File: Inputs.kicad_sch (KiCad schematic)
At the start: 2 parts, among them J14 Conn_01x30_Socket

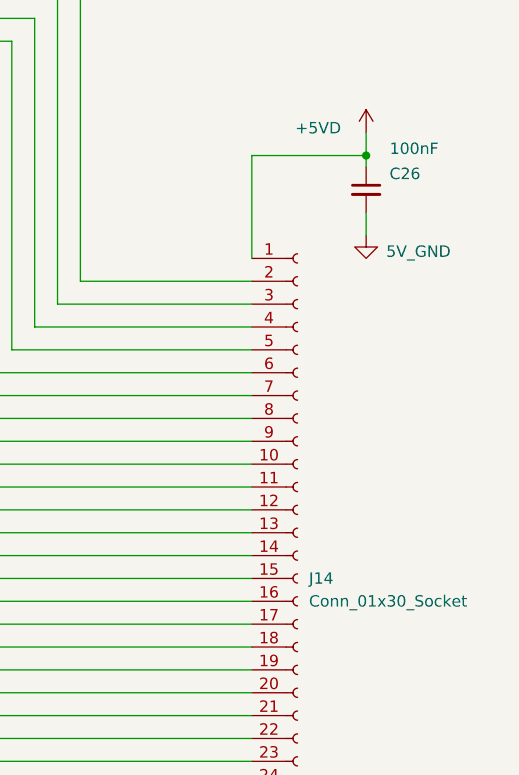
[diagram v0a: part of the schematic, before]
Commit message: Deleted stale test production files. Fixed up a bug with power isolation. Created some footprints for wire to board connectors although ran out of time to fix a bug where they do no lock in. Fixes to readme
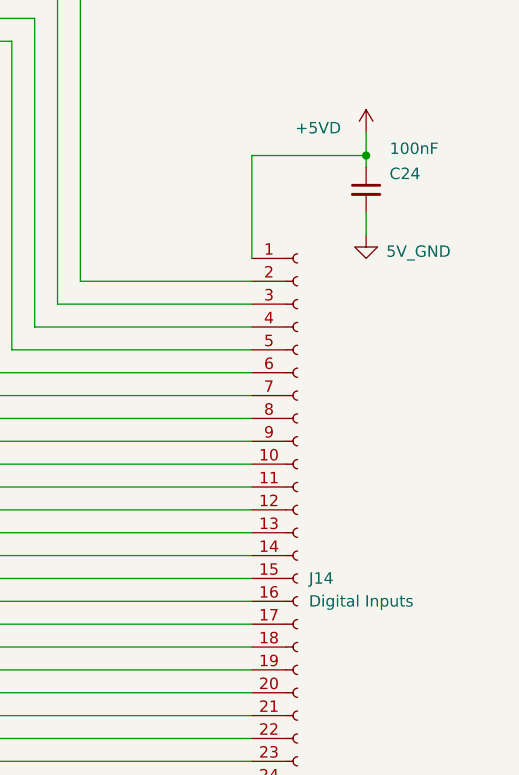
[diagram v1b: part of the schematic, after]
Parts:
- J14: value Conn_01x30_Socket -> Digital Inputs; footprint (none) -> OSTVTerminalBlocks:Conn01x30
- renumbered C26 to C24
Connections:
- net Digital Input ${CH1}&${CH2}/MCU_IP${CH1} is gone; now on net Digital Input ${CH1}&${CH2}/MCU_IP${CH1}: J14.8 (Pin_8)
- net Digital Input ${CH1}&${CH2}/MCU_IP${CH2} is gone; now on net Digital Input ${CH1}&${CH2}/MCU_IP${CH2}: J14.9 (Pin_9)
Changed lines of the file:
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@@
 		(on_board yes)
 		(dnp no)
-		(property "Reference" "#PWR0150"
+		(property "Reference" "#PWR0144"
 			(at 193.04 147.32 0)
 			(effects
@@
 			(project "Remora Nucleo F446ZE Hat"
 				(path "/5473abc6-7b93-43cc-a401-f691c4d7d7cf/181d5939-8311-41b3-8216-f7233e3a75eb"
-					(reference "#PWR0150")
+					(reference "#PWR0144")
 					(unit 1)
 				)
@@
 		(on_board yes)
 		(dnp no)
-		(property "Reference" "#PWR0151"
+		(property "Reference" "#PWR0145"
 			(at 205.74 54.61 0)
 			(effects
@@
 			(project "Remora Nucleo F446ZE Hat"
 				(path "/5473abc6-7b93-43cc-a401-f691c4d7d7cf/181d5939-8311-41b3-8216-f7233e3a75eb"
-					(reference "#PWR0151")
+					(reference "#PWR0145")
 					(unit 1)
 				)
@@
 		(on_board yes)
 		(dnp no)
-		(property "Reference" "C26"
+		(property "Reference" "C24"
 			(at 210.058 55.372 0)
 			(effects
@@
 			(project "Remora Nucleo F446ZE Hat"
 				(path "/5473abc6-7b93-43cc-a401-f691c4d7d7cf/181d5939-8311-41b3-8216-f7233e3a75eb"
-					(reference "C26")
+					(reference "C24")
 					(unit 1)
 				)
@@
 		(on_board yes)
 		(dnp no)
-		(property "Reference" "#PWR0152"
+		(property "Reference" "#PWR0146"
 			(at 205.74 68.58 0)
 			(effects
@@
 			(project "Remora Nucleo F446ZE Hat"
 				(path "/5473abc6-7b93-43cc-a401-f691c4d7d7cf/181d5939-8311-41b3-8216-f7233e3a75eb"
-					(reference "#PWR0152")
+					(reference "#PWR0146")
 					(unit 1)
 				)
@@
 			)
 		)
-		(property "Value" "Conn_01x30_Socket"
+		(property "Value" "Digital Inputs"
 			(at 199.39 102.8699 0)
 			(effects
@@
 			)
 		)
-		(property "Footprint" ""
+		(property "Footprint" "OSTVTerminalBlocks:Conn01x30"
 			(at 198.12 100.33 0)
 			(effects

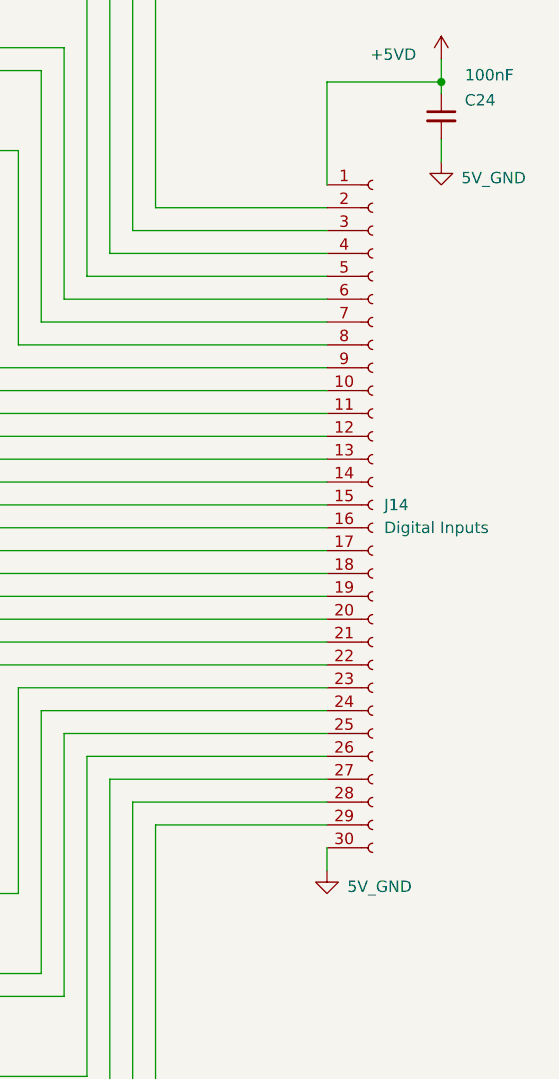
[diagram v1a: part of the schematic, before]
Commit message: restructured power supplies to enable Spindle DAC to be isolated. We now have the option of supplying two 24V inputs, one to power the nucleo and everything logic side and the other to power peripherals. Some testing will be required.
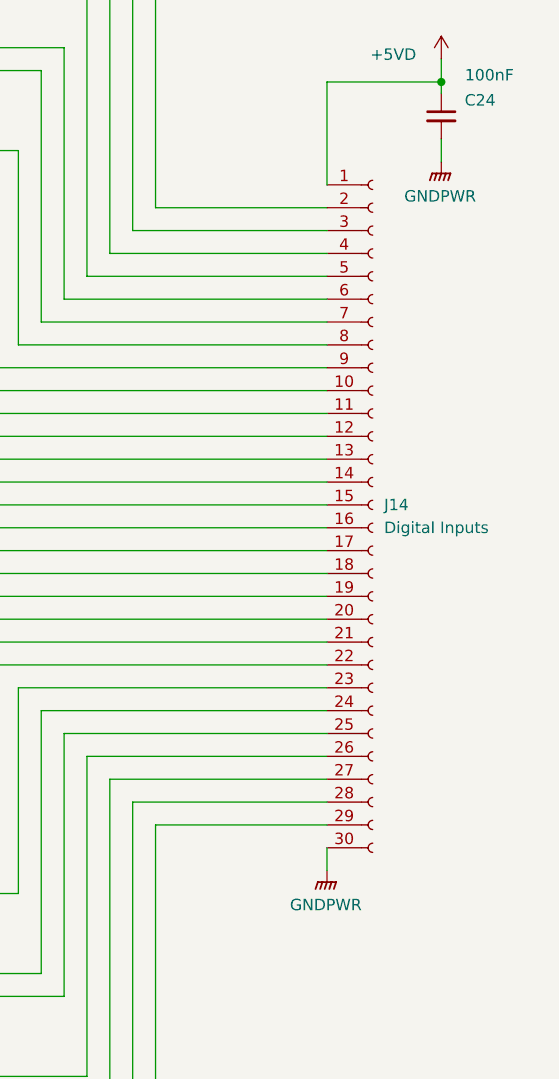
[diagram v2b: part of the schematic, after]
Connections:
- net Digital Input ${CH1}&${CH2}/MCU_IP${CH1} is gone; now on net Digital Input ${CH1}&${CH2}/MCU_IP${CH1}: J14.8 (Pin_8)
- net Digital Input ${CH1}&${CH2}/MCU_IP${CH2} is gone; now on net Digital Input ${CH1}&${CH2}/MCU_IP${CH2}: J14.9 (Pin_9)
- net 5V_GND renamed GNDPWR
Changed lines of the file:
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@@
-	)
-	(symbol
-		(lib_id "power:GND1")
-		(at 193.04 140.97 0)
-		(unit 1)
-		(exclude_from_sim no)
-		(in_bom yes)
-		(on_board yes)
-		(dnp no)
-		(property "Reference" "#PWR0144"
-			(at 193.04 147.32 0)
-			(effects
-				(font
-					(size 1.27 1.27)
-				)
-				(hide yes)
-			)
-		)
-		(property "Value" "5V_GND"
-			(at 198.882 142.748 0)
-			(effects
-				(font
-					(size 1.27 1.27)
-				)
-			)
-		)
-		(property "Footprint" ""
-			(at 193.04 140.97 0)
-			(effects
-				(font
-					(size 1.27 1.27)
-				)
-				(hide yes)
-			)
-		)
-		(property "Datasheet" ""
-			(at 193.04 140.97 0)
-			(effects
-				(font
-					(size 1.27 1.27)
-				)
-				(hide yes)
-			)
-		)
-		(property "Description" "Power symbol creates a global label with name \"GND1\" , ground"
-			(at 193.04 140.97 0)
-			(effects
-				(font
-					(size 1.27 1.27)
-				)
-				(hide yes)
-			)
-		)
-		(pin "1"
-		)
-		(instances
-			(project "Remora Nucleo F446ZE Hat"
-				(path "/5473abc6-7b93-43cc-a401-f691c4d7d7cf/181d5939-8311-41b3-8216-f7233e3a75eb"
-					(reference "#PWR0144")
-					(unit 1)
-				)
-			)
-		)
 	)
 	(symbol
@@
 	)
 	(symbol
+		(lib_id "power:GNDPWR")
+		(at 193.04 140.97 0)
+		(unit 1)
+		(exclude_from_sim no)
+		(in_bom yes)
+		(on_board yes)
+		(dnp no)
+		(fields_autoplaced yes)
+		(property "Reference" "#PWR073"
+			(at 193.04 146.05 0)
+			(effects
+				(font
+					(size 1.27 1.27)
+				)
+				(hide yes)
+			)
+		)
+		(property "Value" "GNDPWR"
+			(at 192.913 144.78 0)
+			(effects
+				(font
+					(size 1.27 1.27)
+				)
+			)
+		)
+		(property "Footprint" ""
+			(at 193.04 142.24 0)
+			(effects
+				(font
+					(size 1.27 1.27)
+				)
+				(hide yes)
+			)
+		)
+		(property "Datasheet" ""
+			(at 193.04 142.24 0)
+			(effects
+				(font
+					(size 1.27 1.27)
+				)
+				(hide yes)
+			)
+		)
+		(property "Description" "Power symbol creates a global label with name \"GNDPWR\" , global ground"
+			(at 193.04 140.97 0)
+			(effects
+				(font
+					(size 1.27 1.27)
+				)
+				(hide yes)
+			)
+		)
+		(pin "1"
+		)
+		(instances
+			(project "Remora Nucleo F446ZE Hat"
+				(path "/5473abc6-7b93-43cc-a401-f691c4d7d7cf/181d5939-8311-41b3-8216-f7233e3a75eb"
+					(reference "#PWR073")
+					(unit 1)
+				)
+			)
+		)
+	)
+	(symbol
 		(lib_id "Device:C_Small")
 		(at 205.74 57.15 0)
@@
 	)
 	(symbol
-		(lib_id "power:GND1")
+		(lib_id "power:GNDPWR")
 		(at 205.74 62.23 0)
 		(unit 1)
@@
 		(on_board yes)
 		(dnp no)
-		(property "Reference" "#PWR0146"
-			(at 205.74 68.58 0)
-			(effects
-				(font
-					(size 1.27 1.27)
-				)
-				(hide yes)
-			)
-		)
-		(property "Value" "5V_GND"
-			(at 215.138 64.008 0)
-			(effects
-				(font
-					(size 1.27 1.27)
-				)
-				(justify right)
+		(fields_autoplaced yes)
+		(property "Reference" "#PWR071"
+			(at 205.74 67.31 0)
+			(effects
+				(font
+					(size 1.27 1.27)
+				)
+				(hide yes)
+			)
+		)
+		(property "Value" "GNDPWR"
+			(at 205.613 66.04 0)
+			(effects
+				(font
+					(size 1.27 1.27)
+				)
 			)
 		)
 		(property "Footprint" ""
+			(at 205.74 63.5 0)
+			(effects
+				(font
+					(size 1.27 1.27)
+				)
+				(hide yes)
+			)
+		)
+		(property "Datasheet" ""
+			(at 205.74 63.5 0)
+			(effects
+				(font
+					(size 1.27 1.27)
+				)
+				(hide yes)
+			)
+		)
+		(property "Description" "Power symbol creates a global label with name \"GNDPWR\" , global ground"
 			(at 205.74 62.23 0)
 			(effects
@@
 			)
 		)
-		(property "Datasheet" ""
-			(at 205.74 62.23 0)
-			(effects
-				(font
-					(size 1.27 1.27)
-				)
-				(hide yes)
-			)
-		)
-		(property "Description" "Power symbol creates a global label with name \"GND1\" , ground"
-			(at 205.74 62.23 0)
-			(effects
-				(font
-					(size 1.27 1.27)
-				)
-				(hide yes)
-			)
-		)
-		(pin "1"
-		)
-		(instances
-			(project "Remora Nucleo F446ZE Hat"
-				(path "/5473abc6-7b93-43cc-a401-f691c4d7d7cf/181d5939-8311-41b3-8216-f7233e3a75eb"
-					(reference "#PWR0146")
-					(unit 1)
-				)
+		(pin "1"
+		)
+		(instances
+			(project "Remora Nucleo F446ZE Hat"
+				(path "/5473abc6-7b93-43cc-a401-f691c4d7d7cf/181d5939-8311-41b3-8216-f7233e3a75eb"
+					(reference "#PWR071")
+					(unit 1)
+				)

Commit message: Fixes to screw terminal footprints, updated BOM and included in project folder
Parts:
- J14: footprint OSTVTerminalBlocks:Conn01x30 -> EBWA_06_A:CONN_EBWA-30-A_ADM
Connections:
- net Digital Input ${CH1}&${CH2}/MCU_IP${CH1} is gone; now on net Digital Input ${CH1}&${CH2}/MCU_IP${CH1}: J14.8 (Pin_8)
- net Digital Input ${CH1}&${CH2}/MCU_IP${CH2} is gone; now on net Digital Input ${CH1}&${CH2}/MCU_IP${CH2}: J14.9 (Pin_9)
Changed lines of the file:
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@@
 			)
 		)
-		(property "Footprint" "OSTVTerminalBlocks:Conn01x30"
+		(property "Footprint" "EBWA_06_A:CONN_EBWA-30-A_ADM"
 			(at 198.12 100.33 0)
 			(effects

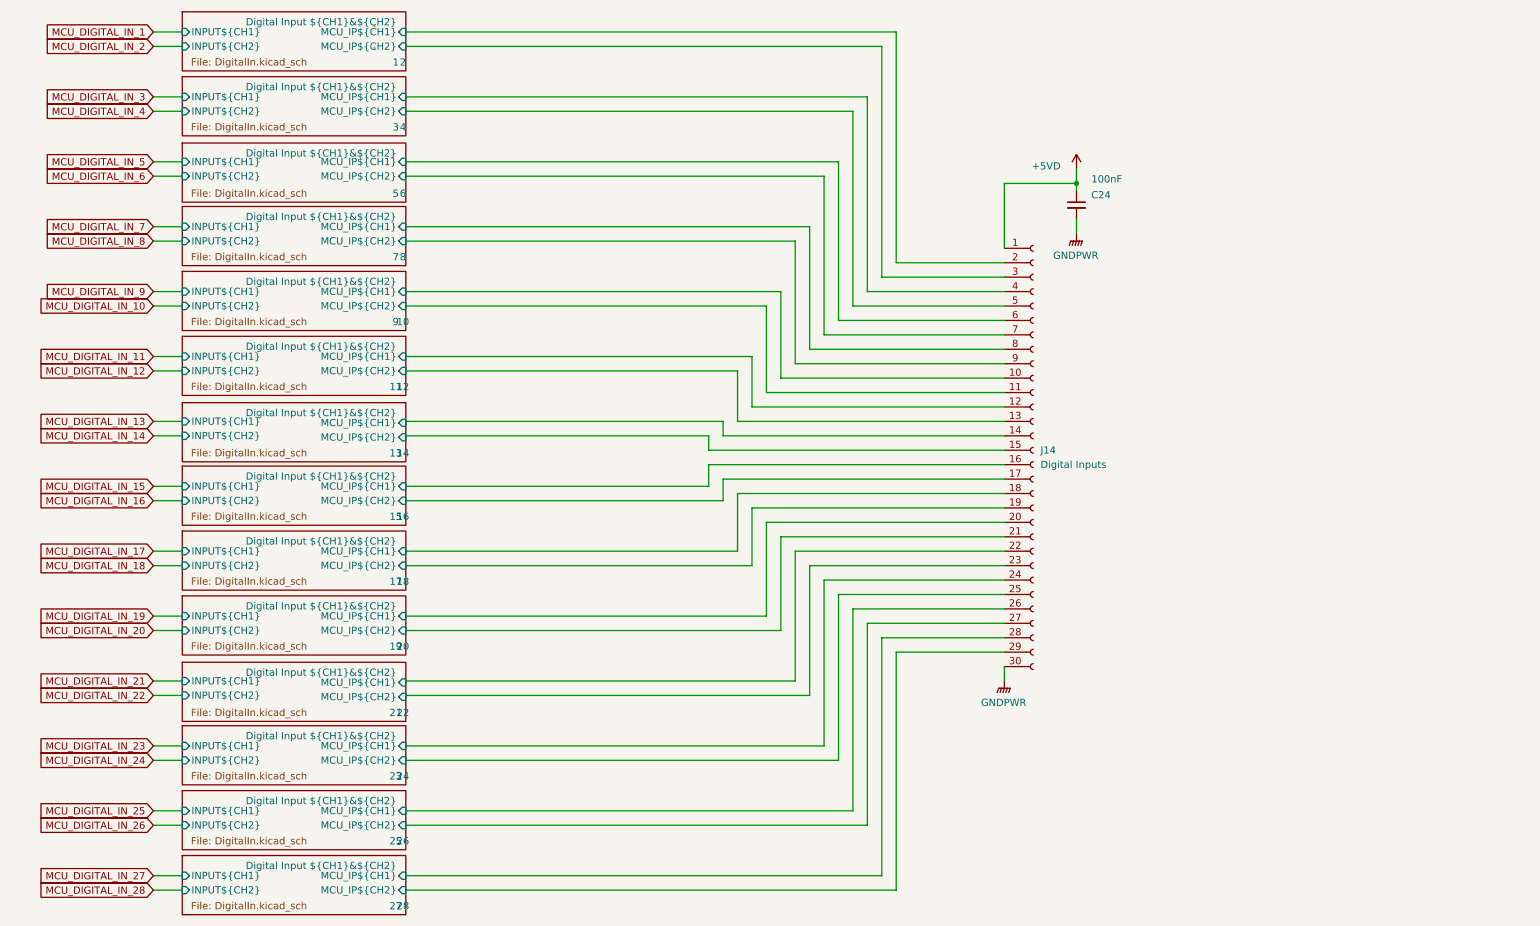
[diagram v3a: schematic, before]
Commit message: updates to read me, marked V1 parts inactive and made start on board layout for initial test board. fixes to BOM to suit
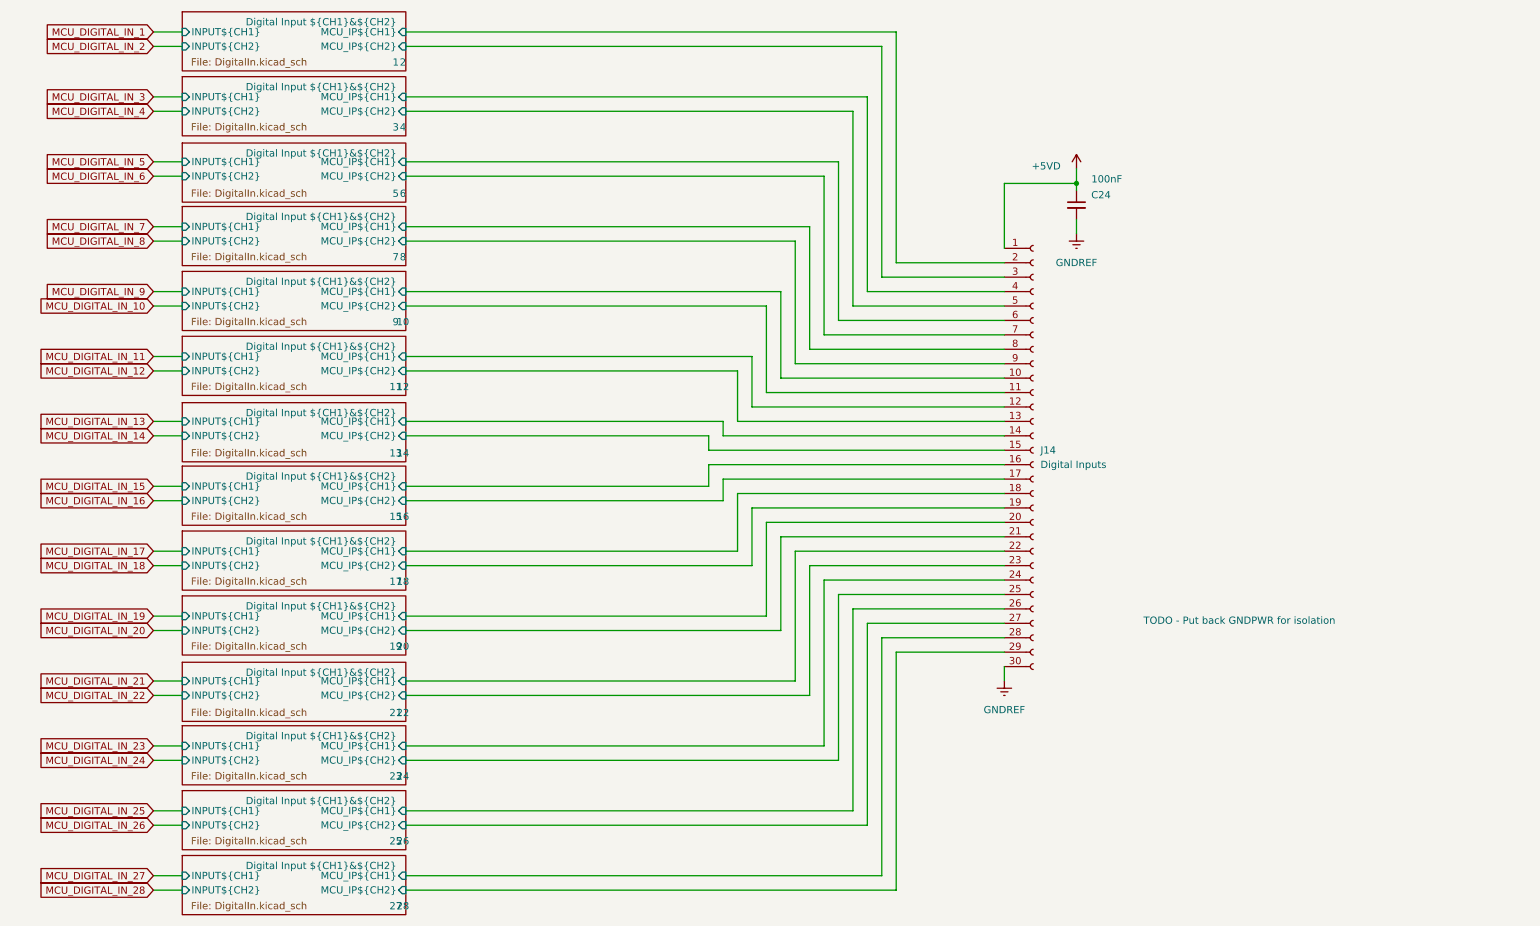
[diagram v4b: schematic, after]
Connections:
- net Digital Input ${CH1}&${CH2}/MCU_IP${CH1} is gone; now on net Digital Input ${CH1}&${CH2}/MCU_IP${CH1}: J14.8 (Pin_8)
- net Digital Input ${CH1}&${CH2}/MCU_IP${CH2} is gone; now on net Digital Input ${CH1}&${CH2}/MCU_IP${CH2}: J14.9 (Pin_9)
- net Digital Input ${CH1}&${CH2}/MCU_IP${CH1}: now reaches J14.14 (Pin_14)
- net Digital Input ${CH1}&${CH2}/MCU_IP${CH2}: now reaches J14.15 (Pin_15)
- net Digital Input ${CH1}&${CH2}/MCU_IP${CH1}: now reaches J14.22 (Pin_22)
- net Digital Input ${CH1}&${CH2}/MCU_IP${CH2}: now reaches J14.23 (Pin_23)
- net GNDPWR renamed GNDREF
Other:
- note added: "TODO - Put back GNDPWR for isolation"
